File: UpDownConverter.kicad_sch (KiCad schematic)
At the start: 0 parts

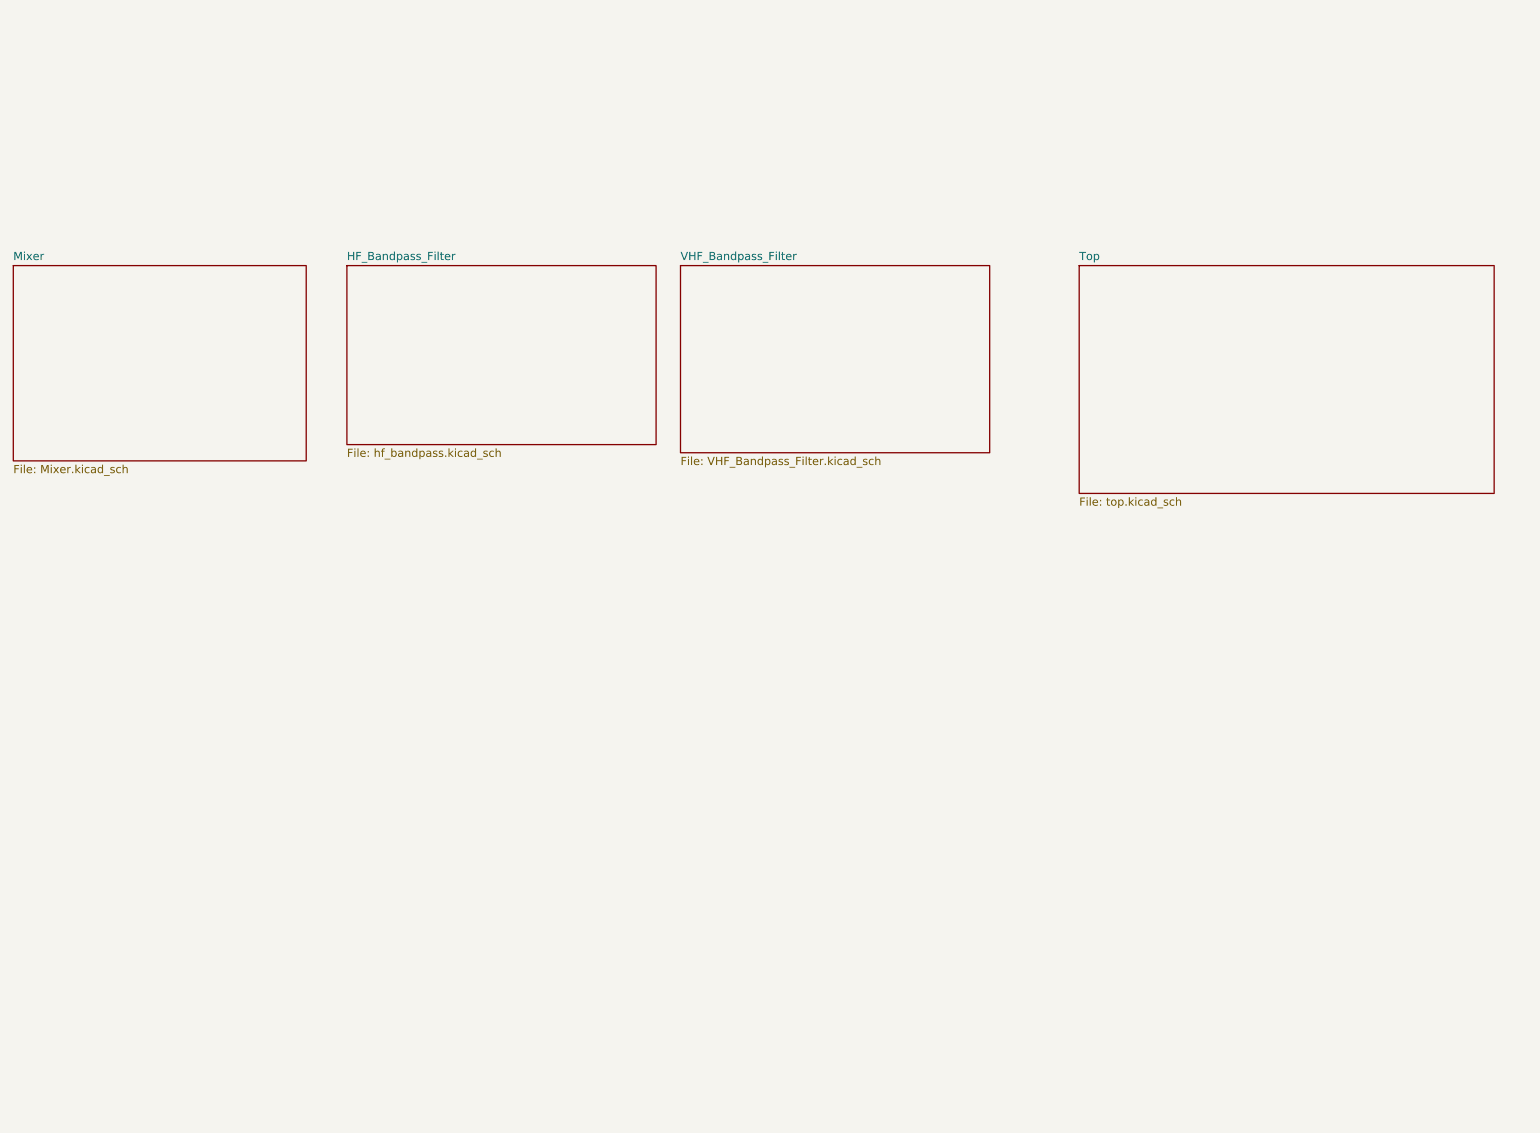
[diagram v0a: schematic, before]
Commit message: Redefined filters & Top Level Diagram
- Implement wider filters to accomodate 10% tolerance parts.
- Break design in to top-level heirarchical blocks.
- Start wiring some of the blocks together.
- Add L-Band segment, but is currently just a copy of the UHF filter.
- Add the start of a TX path.
- Add placeholders for power and band/tune control.
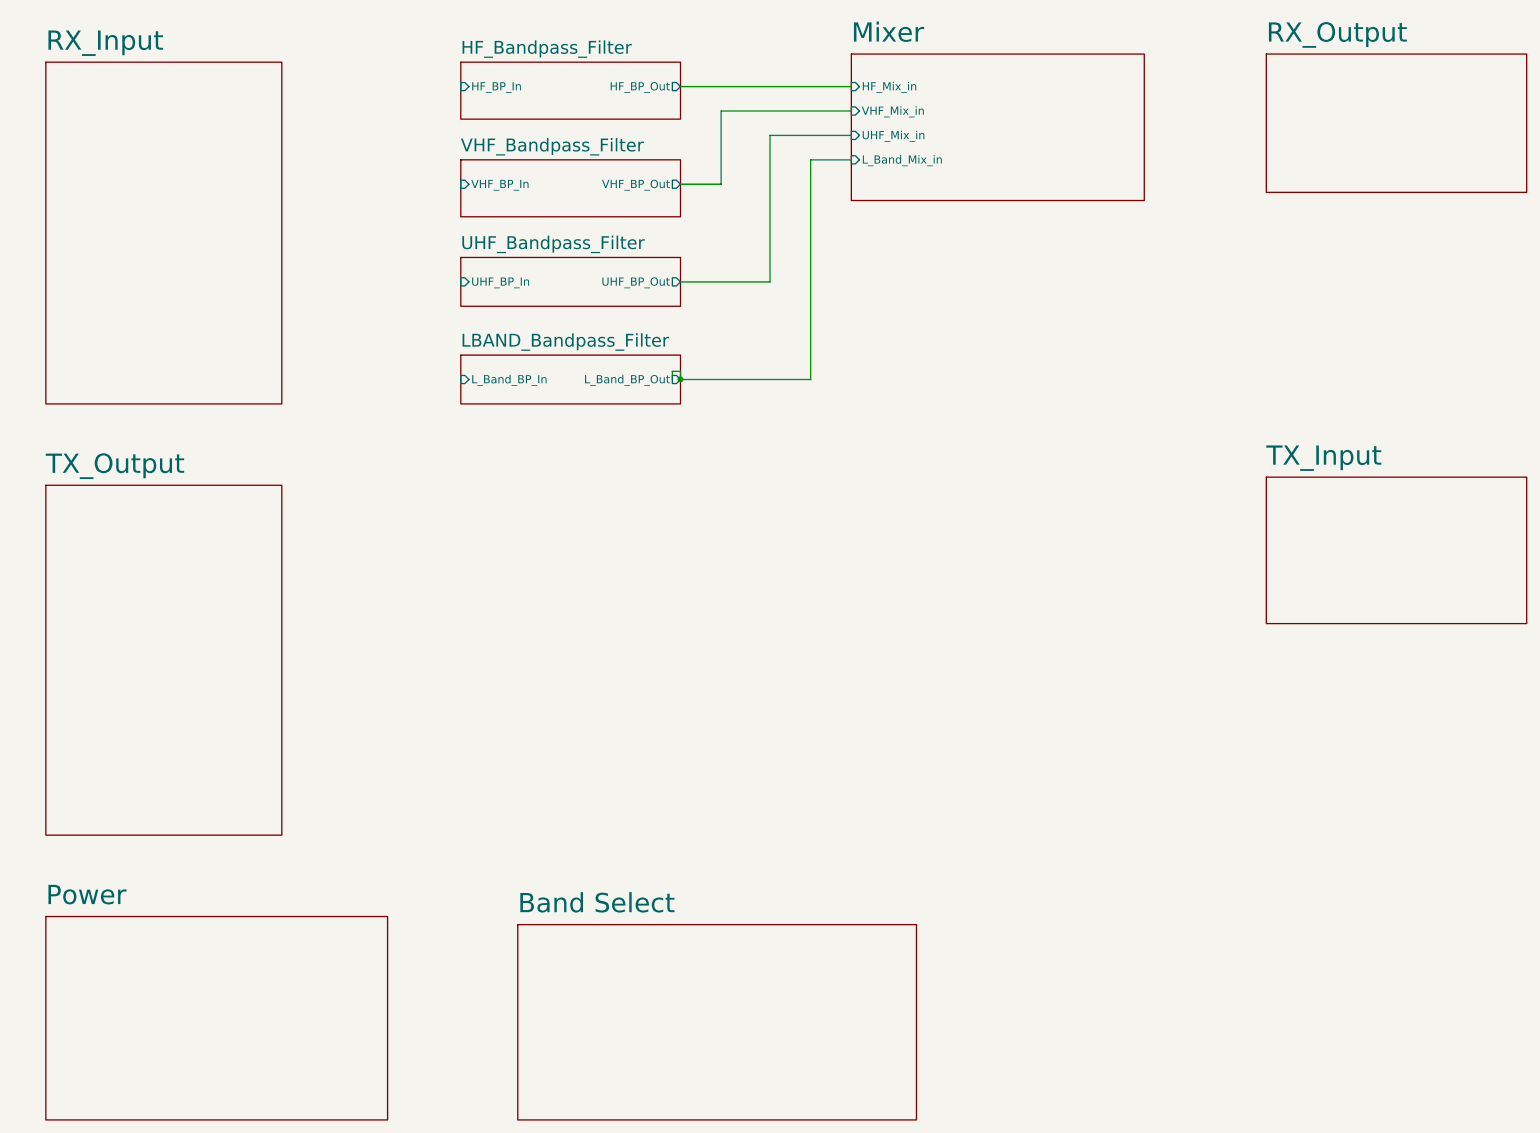
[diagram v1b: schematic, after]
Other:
- removed sheet Top
- added sheet Band Select (band_select.kicad_sch)
- added sheet LBAND_Bandpass_Filter (lband_bp_filter.kicad_sch)
- added sheet Power (power.kicad_sch)
- added sheet RX_Input (RX_Input.kicad_sch)
- added sheet RX_Output (rx_output.kicad_sch)
- added sheet TX_Input (tx_input.kicad_sch)
- added sheet TX_Output (tx_output.kicad_sch)
- added sheet UHF_Bandpass_Filter (uhf_bandpass_filter.kicad_sch)
- sheet HF_Bandpass_Filter ports: added HF_BP_In, HF_BP_Out; removed none
- sheet Mixer ports: added HF_Mix_in, L_Band_Mix_in, UHF_Mix_in, VHF_Mix_in; removed none
- sheet VHF_Bandpass_Filter ports: added VHF_BP_In, VHF_BP_Out; removed none

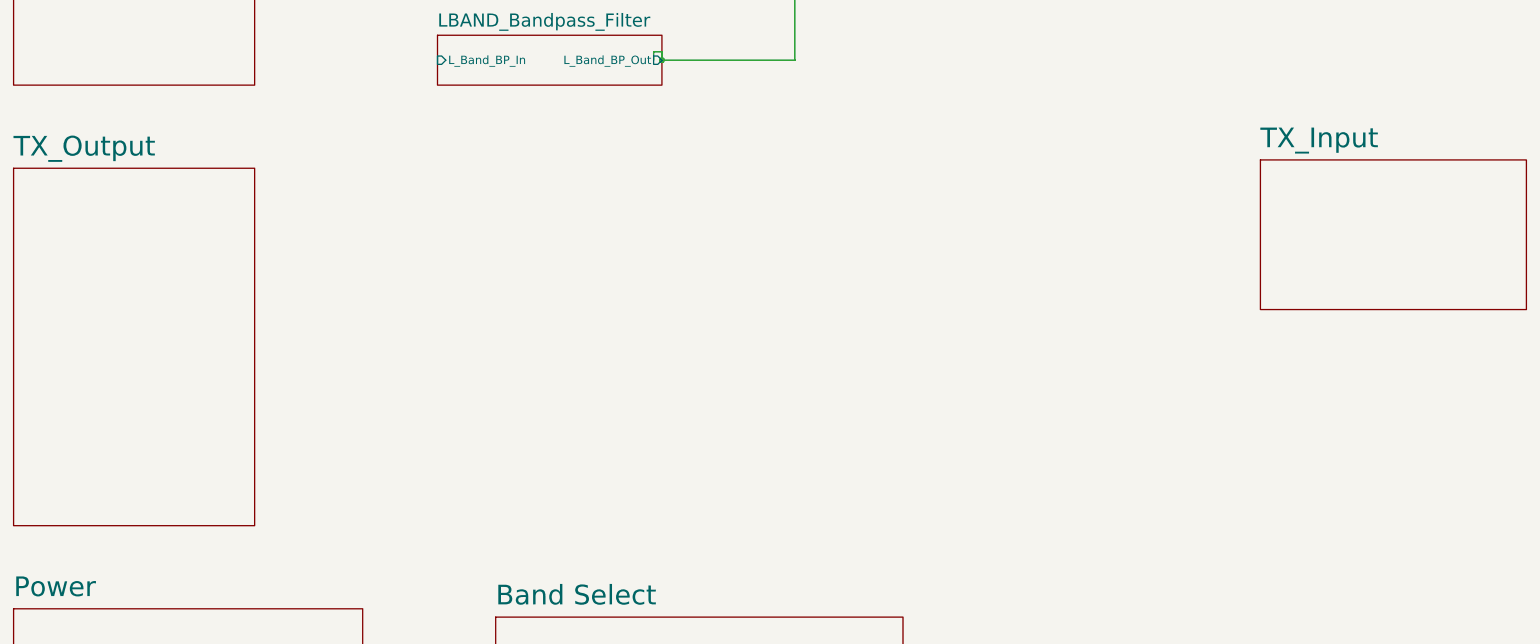
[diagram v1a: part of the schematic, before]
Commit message: More filter work. Add project title to drawings.
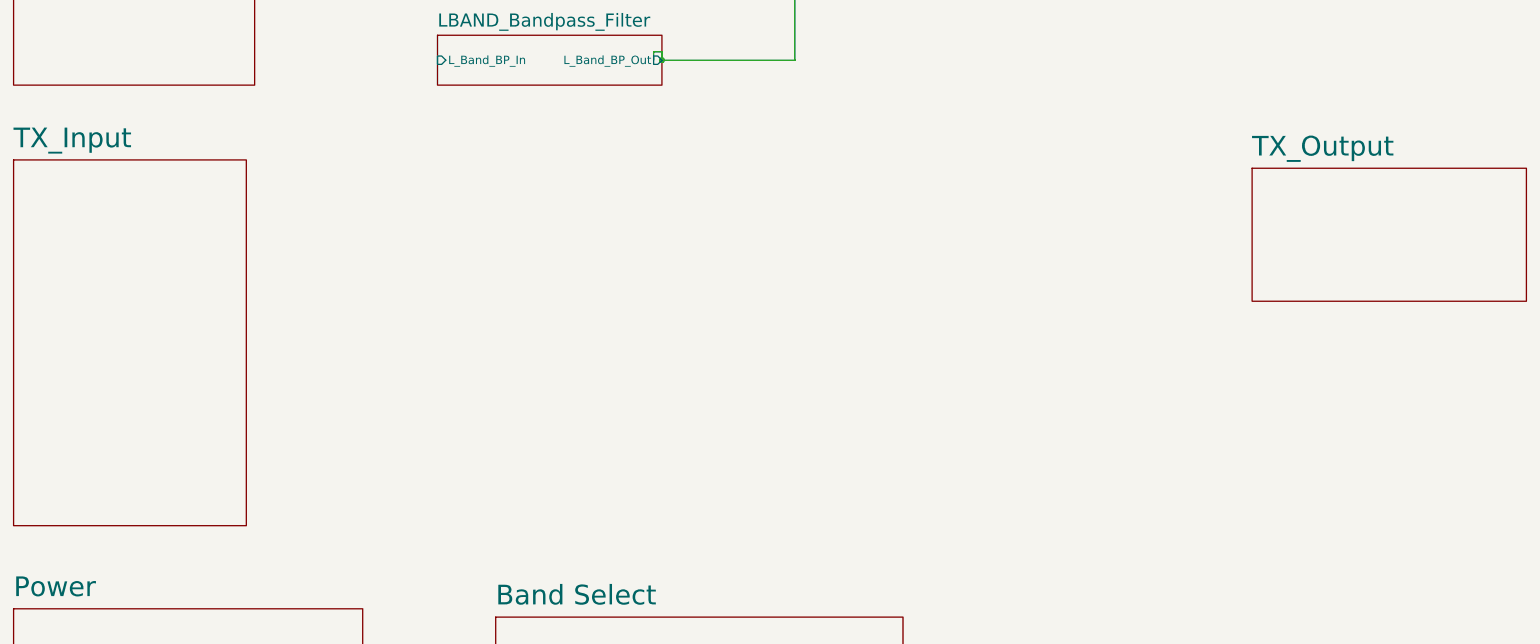
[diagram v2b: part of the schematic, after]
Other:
- company: (none) -> Steves Custom Computers
- title: (none) -> PLUTO RF Card Front-End
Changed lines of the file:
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@@
 (kicad_sch (version 20230121) (generator eeschema)
   (paper "A4")
+  (title_block
+    (title "PLUTO RF Card Front-End")
+    (rev " 001")
+    (company "Steves Custom Computers")
+  )
   (junction (at 123.19 73.66) (diameter 0) (color 0 0 0 0)
   )
@@
     (stroke (width 0) (type default))
   )
-  (sheet (at 214.63 88.9) (size 40.64 22.86) (fields_autoplaced)
+  (sheet (at 24.13 88.9) (size 35.56 55.88) (fields_autoplaced)
     (stroke (width 0.1524) (type solid))
     (fill (color 0 0 0 0.0000))
-    (property "Sheetname" "TX_Input" (at 214.63 87.3234 0)
+    (property "Sheetname" "TX_Input" (at 24.13 87.3234 0)
       (effects (font (size 3 3)) (justify left bottom))
     )
-    (property "Sheetfile" "tx_input.kicad_sch" (at 214.63 112.3446 0)
+    (property "Sheetfile" "tx_input.kicad_sch" (at 24.13 145.3646 0)
       (effects (font (size 1.27 1.27)) (justify left top) hide)
     )
@@
     )
   )
-  (sheet (at 24.13 90.17) (size 36.83 54.61) (fields_autoplaced)
+  (sheet (at 213.36 90.17) (size 41.91 20.32) (fields_autoplaced)
     (stroke (width 0.1524) (type solid))
     (fill (color 0 0 0 0.0000))
-    (property "Sheetname" "TX_Output" (at 24.13 88.5934 0)
+    (property "Sheetname" "TX_Output" (at 213.36 88.5934 0)
       (effects (font (size 3 3)) (justify left bottom))
     )
-    (property "Sheetfile" "tx_output.kicad_sch" (at 24.13 145.3646 0)
+    (property "Sheetfile" "tx_output.kicad_sch" (at 213.36 111.0746 0)
       (effects (font (size 1.27 1.27)) (justify left top) hide)
     )

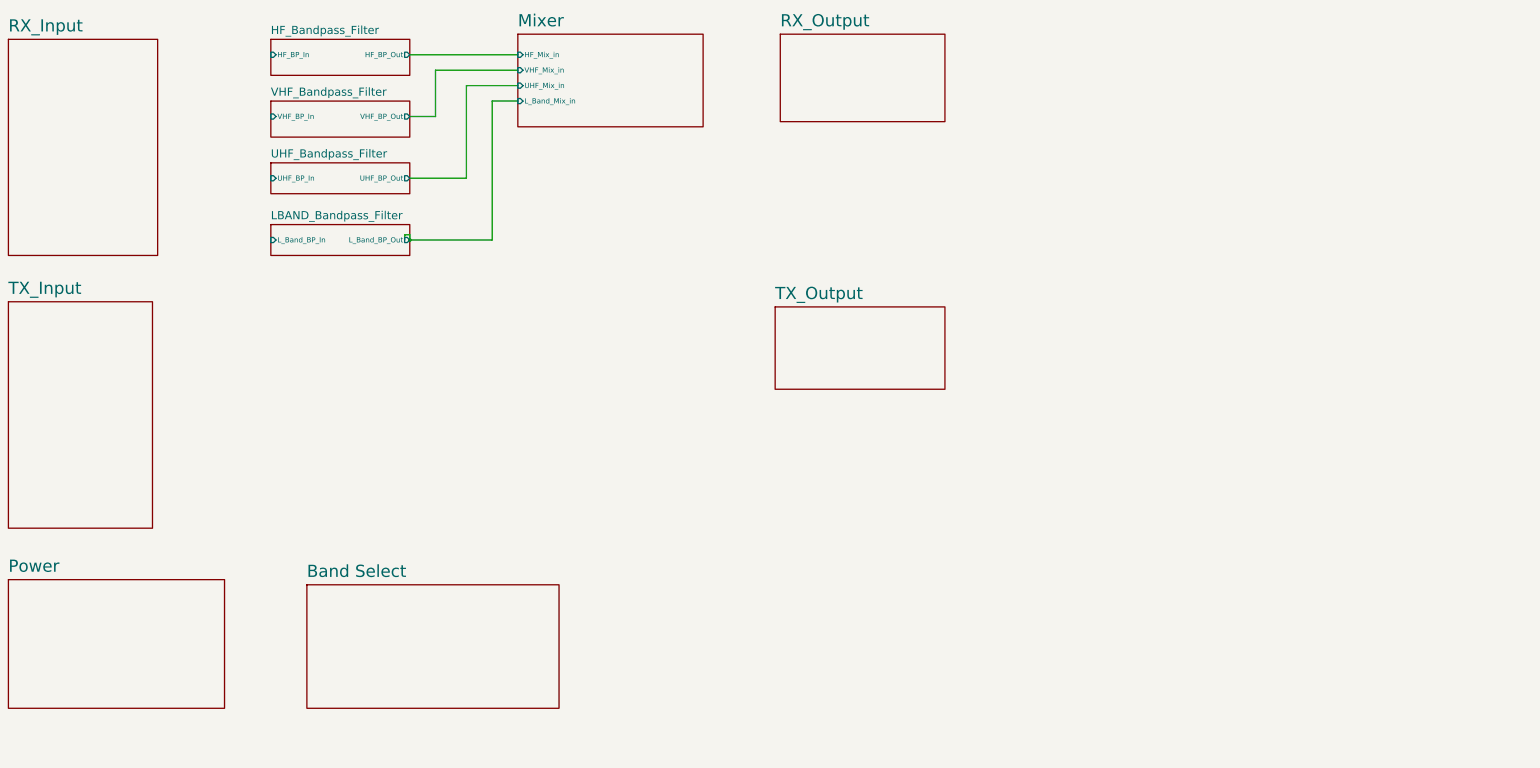
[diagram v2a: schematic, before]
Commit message: Major restructure. Add power/control busses.
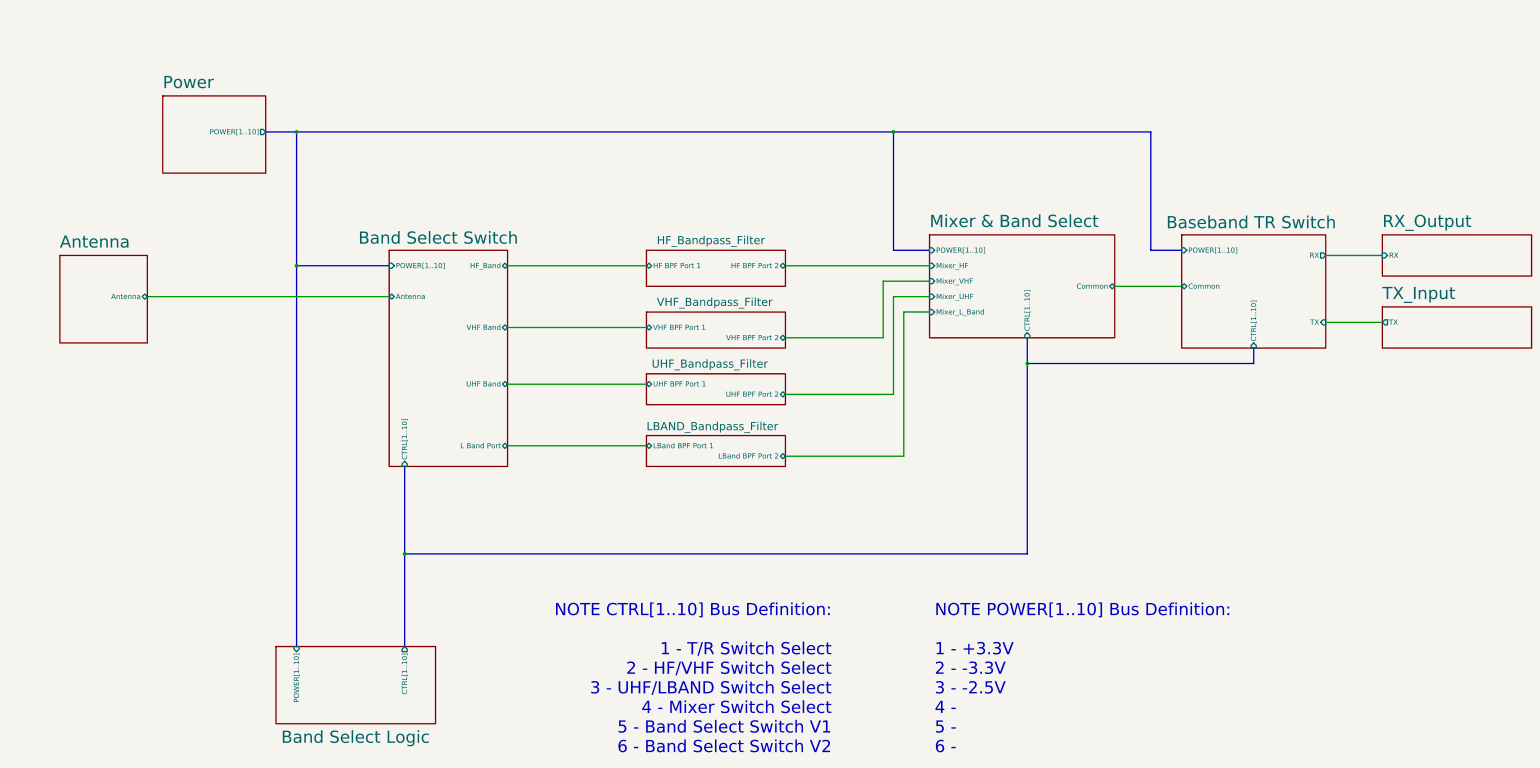
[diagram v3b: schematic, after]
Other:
- sheet Band Select renamed Band Select Logic
- sheet Mixer renamed Mixer & Band Select
- sheet RX_Input renamed Antenna
- removed sheet TX_Output
- added sheet Band Select Switch (rf_tr_switch.kicad_sch)
- added sheet Baseband TR Switch (bb_tr_switch.kicad_sch)
- sheet Antenna ports: added Antenna; removed none
- sheet Band Select Logic ports: added CTRL[1..10], POWER[1..10]; removed none
- sheet HF_Bandpass_Filter ports: added HF BPF Port 1, HF BPF Port 2; removed HF_BP_In, HF_BP_Out
- sheet LBAND_Bandpass_Filter ports: added LBand BPF Port 1, LBand BPF Port 2; removed L_Band_BP_In, L_Band_BP_Out
- sheet Mixer & Band Select ports: added CTRL[1..10], Common, Mixer_HF, Mixer_L_Band, Mixer_UHF, Mixer_VHF, POWER[1..10]; removed HF_Mix_in, L_Band_Mix_in, UHF_Mix_in, VHF_Mix_in
- sheet Power ports: added POWER[1..10]; removed none
- sheet RX_Output ports: added RX; removed none
- sheet TX_Input ports: added TX; removed none
- sheet UHF_Bandpass_Filter ports: added UHF BPF Port 1, UHF BPF Port 2; removed UHF_BP_In, UHF_BP_Out
- sheet VHF_Bandpass_Filter ports: added VHF BPF Port 1, VHF BPF Port 2; removed VHF_BP_In, VHF_BP_Out
- note added: "NOTE CTRL[1..10] Bus Definition: 1 - T/R Switch Select 2 - HF/VHF Switch Select 3 - UHF/LBAND Switch Select 4 - Mixer Switch Select 5 - Band Select Switch V1 6 - Band Select Switch V2"
- note added: "NOTE POWER[1..10] Bus Definition: 1 - +3.3V 2 - -3.3V 3 - -2.5V 4 - 5 - 6 -"
- title: PLUTO RF Card Front-End -> PLUTO RF Front-End Card
